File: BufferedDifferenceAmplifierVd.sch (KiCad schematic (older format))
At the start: 13 parts, among them U1 LMC6044, U2 LMC6044, U3 LM324

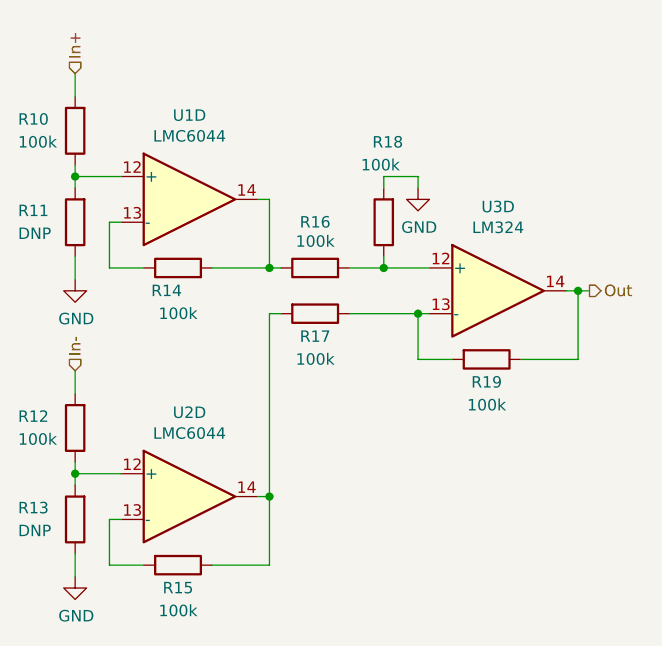
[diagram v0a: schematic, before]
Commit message: Added negative swing on gate-source bias and RTD connection.
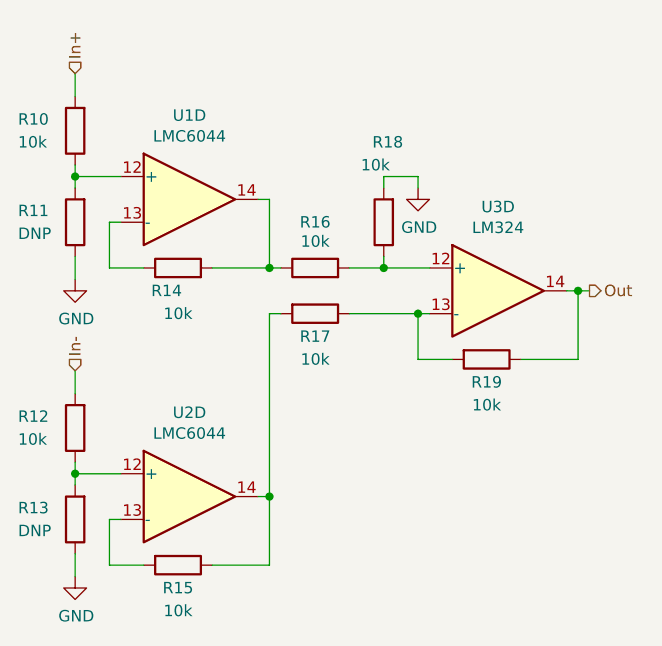
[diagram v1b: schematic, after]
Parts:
- R10, R12, R14, R15, R16, R17, R18, R19: value 100k -> 10k
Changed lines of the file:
@@
 AR Path="/5F4EF06B/5F4F2F13" Ref="R?"  Part="1"
 F 0 "R10" H 5400 2700 50  0000 R CNN
-F 1 "100k" H 5400 2800 50  0000 R CNN
+F 1 "10k" H 5400 2800 50  0000 R CNN
 F 2 "Resistor_SMD:R_0603_1608Metric" V 5080 2750 50  0001 C CNN
 F 3 "~" H 5150 2750 50  0001 C CNN
@@
 AR Path="/5F4EF06B/5F4F5394" Ref="R?"  Part="1"
 F 0 "R14" V 5500 3400 50  0000 C CNN
-F 1 "100k" V 5400 3350 50  0000 C CNN
+F 1 "10k" V 5400 3350 50  0000 C CNN
 F 2 "Resistor_SMD:R_0603_1608Metric" V 5530 3350 50  0001 C CNN
 F 3 "~" H 5600 3350 50  0001 C CNN
@@
 AR Path="/5F4EF06B/5F4F2F19" Ref="R?"  Part="1"
 F 0 "R16" V 6400 3350 50  0000 C CNN
-F 1 "100k" V 6316 3350 50  0000 C CNN
+F 1 "10k" V 6316 3350 50  0000 C CNN
 F 2 "Resistor_SMD:R_0603_1608Metric" V 6130 3350 50  0001 C CNN
 F 3 "~" H 6200 3350 50  0001 C CNN
@@
 AR Path="/5F4EF06B/5F4F2F1B" Ref="R?"  Part="1"
 F 0 "R12" H 5400 4000 50  0000 R CNN
-F 1 "100k" H 5400 4100 50  0000 R CNN
+F 1 "10k" H 5400 4100 50  0000 R CNN
 F 2 "Resistor_SMD:R_0603_1608Metric" V 5080 4050 50  0001 C CNN
 F 3 "~" H 5150 4050 50  0001 C CNN
@@
 AR Path="/5F4EF06B/5F4F2128" Ref="R?"  Part="1"
 F 0 "R17" V 6300 3550 50  0000 C CNN
-F 1 "100k" V 6400 3550 50  0000 C CNN
+F 1 "10k" V 6400 3550 50  0000 C CNN
 F 2 "Resistor_SMD:R_0603_1608Metric" V 6130 3550 50  0001 C CNN
 F 3 "~" H 6200 3550 50  0001 C CNN
@@
 AR Path="/5F4EF06B/5F4F2129" Ref="R?"  Part="1"
 F 0 "R19" V 7050 3750 50  0000 C CNN
-F 1 "100k" V 7150 3750 50  0000 C CNN
+F 1 "10k" V 7150 3750 50  0000 C CNN
 F 2 "Resistor_SMD:R_0603_1608Metric" V 6880 3750 50  0001 C CNN
 F 3 "~" H 6950 3750 50  0001 C CNN
@@
 AR Path="/5F4EF06B/5F4F212A" Ref="R?"  Part="1"
 F 0 "R18" H 6550 2800 50  0000 R CNN
-F 1 "100k" H 6600 2900 50  0000 R CNN
+F 1 "10k" H 6600 2900 50  0000 R CNN
 F 2 "Resistor_SMD:R_0603_1608Metric" V 6430 3150 50  0001 C CNN
 F 3 "~" H 6500 3150 50  0001 C CNN
@@
 AR Path="/5F4EF06B/5F4F212B" Ref="R?"  Part="1"
 F 0 "R15" V 5700 4650 50  0000 C CNN
-F 1 "100k" V 5800 4650 50  0000 C CNN
+F 1 "10k" V 5800 4650 50  0000 C CNN
 F 2 "Resistor_SMD:R_0603_1608Metric" V 5530 4650 50  0001 C CNN
 F 3 "~" H 5600 4650 50  0001 C CNN
